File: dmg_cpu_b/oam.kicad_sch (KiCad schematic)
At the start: 134 parts

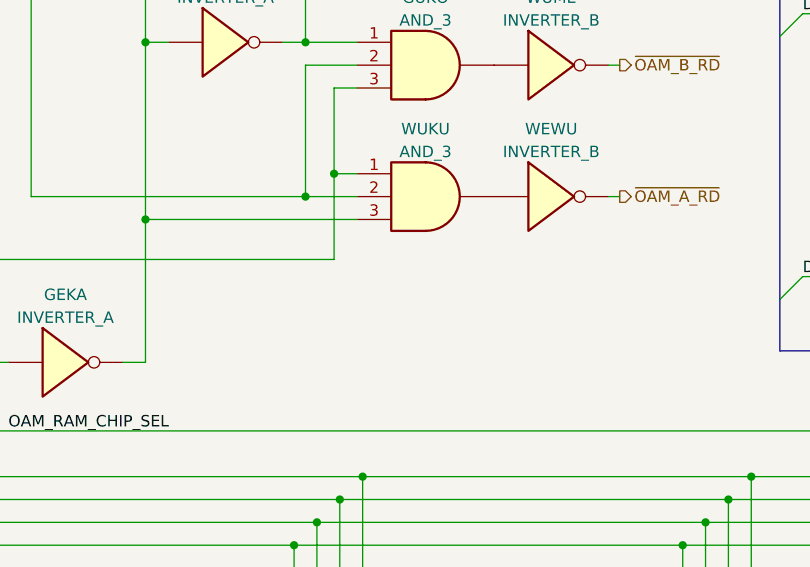
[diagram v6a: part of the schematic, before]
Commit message: All connections between sheet are complete. Can still do with a good tidy up.
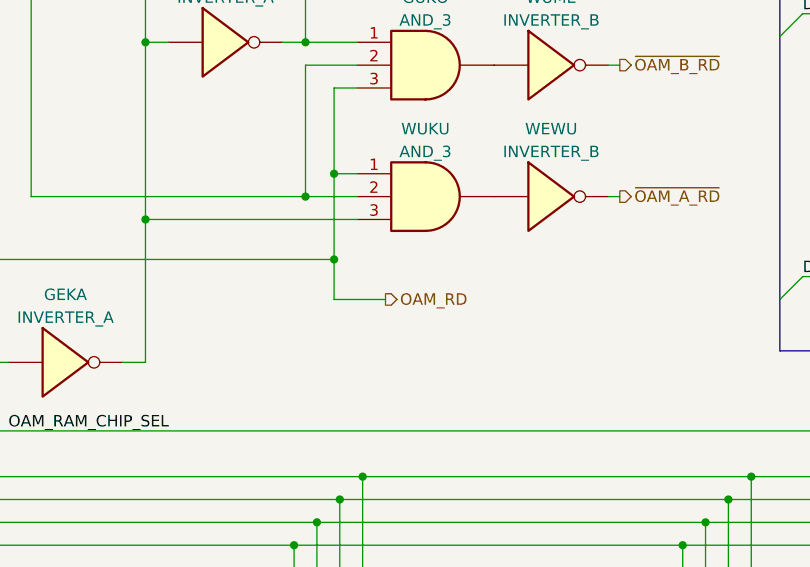
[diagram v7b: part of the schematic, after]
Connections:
- net OAM_RD: now reaches GUKO.3, LEKO.2, WUKU.1
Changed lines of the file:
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@@
   (junction (at 99.06 153.035) (diameter 0) (color 0 0 0 0)
   )
+  (junction (at 182.245 128.905) (diameter 0) (color 0 0 0 0)
+  )
   (junction (at 285.115 51.435) (diameter 0) (color 0 0 0 0)
   )
@@
     (stroke (width 0) (type default) (color 0 0 0 0))
   )
+  (wire (pts (xy 182.245 133.35) (xy 187.96 133.35))
+    (stroke (width 0) (type default) (color 0 0 0 0))
+  )
   (wire (pts (xy 134.62 210.185) (xy 166.37 210.185))
     (stroke (width 0) (type default) (color 0 0 0 0))
@@
     (stroke (width 0) (type default) (color 0 0 0 0))
   )
+  (wire (pts (xy 182.245 128.905) (xy 182.245 133.35))
+    (stroke (width 0) (type default) (color 0 0 0 0))
+  )
   (bus (pts (xy 86.36 208.28) (xy 86.36 223.52))
     (stroke (width 0) (type default) (color 0 0 0 0))
@@
     (effects (font (size 1.27 1.27)) (justify left))
   )
+  (hierarchical_label "OAM_RD" (shape output) (at 187.96 133.35 0)
+    (effects (font (size 1.27 1.27)) (justify left))
+  )
   (hierarchical_label "FEXX" (shape input) (at 92.075 52.705 180)
     (effects (font (size 1.27 1.27)) (justify right))
@@
   (symbol (lib_id "power:+5V") (at 386.08 172.72 0) (unit 1)
     (in_bom yes) (on_board yes) (fields_autoplaced)
-    (property "Reference" "#PWR?" (id 0) (at 386.08 176.53 0)
+    (property "Reference" "#PWR0116" (id 0) (at 386.08 176.53 0)
       (effects (font (size 1.27 1.27)) hide)
     )
@@
   (symbol (lib_id "power:GND") (at 358.14 187.325 0) (unit 1)
     (in_bom yes) (on_board yes) (fields_autoplaced)
-    (property "Reference" "#PWR?" (id 0) (at 358.14 193.675 0)
+    (property "Reference" "#PWR0118" (id 0) (at 358.14 193.675 0)
       (effects (font (size 1.27 1.27)) hide)
     )
@@
   (symbol (lib_id "power:+5V") (at 358.14 172.72 0) (unit 1)
     (in_bom yes) (on_board yes) (fields_autoplaced)
-    (property "Reference" "#PWR?" (id 0) (at 358.14 176.53 0)
+    (property "Reference" "#PWR0117" (id 0) (at 358.14 176.53 0)
       (effects (font (size 1.27 1.27)) hide)
     )
@@
   (symbol (lib_id "power:GND") (at 386.08 187.325 0) (unit 1)
     (in_bom yes) (on_board yes) (fields_autoplaced)
-    (property "Reference" "#PWR?" (id 0) (at 386.08 193.675 0)
+    (property "Reference" "#PWR0115" (id 0) (at 386.08 193.675 0)
       (effects (font (size 1.27 1.27)) hide)
     )
@@
   (symbol (lib_id "power:+5V") (at 26.67 167.64 0) (unit 1)
     (in_bom yes) (on_board yes) (fields_autoplaced)
-    (property "Reference" "#PWR?" (id 0) (at 26.67 171.45 0)
+    (property "Reference" "#PWR0114" (id 0) (at 26.67 171.45 0)
       (effects (font (size 1.27 1.27)) hide)
     )

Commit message: Changes made on review.
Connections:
- net ~{OAM_CS} renamed ~{OAM_OE}
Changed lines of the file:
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@@
     (effects (font (size 1.27 1.27)) (justify left bottom))
   )
-  (label "~{OAM_CS}" (at 187.325 278.765 0)
+  (label "~{OAM_OE}" (at 187.325 278.765 0)
     (effects (font (size 1.27 1.27)) (justify left bottom))
   )
@@
     (effects (font (size 1.27 1.27)) (justify left bottom))
   )
-  (label "~{OAM_CS}" (at 175.895 276.86 180)
+  (label "~{OAM_OE}" (at 175.895 276.86 180)
     (effects (font (size 1.27 1.27)) (justify right bottom))
   )
@@
     (effects (font (size 1.27 1.27)) (justify right bottom))
   )
-  (label "~{OAM_CS}" (at 238.125 278.765 0)
-    (effects (font (size 1.27 1.27)) (justify left bottom))
-  )
+  (label "~{OAM_OE}" (at 238.125 278.765 0)
+    (effects (font (size 1.27 1.27)) (justify left bottom))
+  )
